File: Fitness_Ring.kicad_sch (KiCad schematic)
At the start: 14 parts, among them U1 NRF52832-QFAA-R, U2 MAX30102, U3 MIC5370-SGYMT-TR, U4 MCP73831-2-OT, U5 TXS0102DQE

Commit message: made changes to schematic
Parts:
- added C10: 1.2pF, symbol Device:C
- added C11: 0.1uF, symbol Device:C
- added C12, C9: 100pF, symbol Device:C
- added C6: 100nF, symbol Device:C
- added C7, C8: 12pF, symbol Device:C
- added E1: 2450AT18B100E, 2450AT18B100E:XDCR_2450AT18B100E, symbol New_Library:2450AT18B100E
- added L1: 3.3nH, symbol Device:L
- added L2: 2.7nH, symbol Device:L
- added R4, R5, R6, R7: 4.7K, symbol Device:R
- added U6: MAX30205MTA_, MAX30205MTA_:SON65P300X300X80-9N, symbol New_Library:MAX30205MTA_
- added Y1: 32.768kHz, symbol Device:Crystal
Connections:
- net VSS is gone; now on net GND: U1.31 (VSS), U1.45 (VSS)
- net +3.3V: now also C11.2, R4.1, R5.1, R6.2, U6.8 (VDD)
- net GND: now also U4.2 (V_{SS}), C10.2, C11.1, C6.2, C7.2, C8.2, C9.2, L2.1, R7.2, U6.4 (GND), U6.5 (A2), U6.6 (A1), U6.7 (A0), U6.9 (EP)
- net SCL: now also U1.15 (P0_12), R5.2, U6.2 (SCL); no longer MT1.13 (AP_SCL/AP_SCLK), R1.2
- net SDA: now also U1.14 (P0_11), R4.2, U6.1 (SDA); no longer MT1.14 (AP_SDA/AP_SDIO/AP_SDI), R2.2
- net at U4.5 (PROG): now also R7.1
- net SCLK: now reaches U1.28 (P0_23)
- net SCLK: now also MT1.13 (AP_SCL/AP_SCLK), R1.2
- net SDI: now reaches U1.29 (P0_24)
- net SDI: now also MT1.14 (AP_SDA/AP_SDIO/AP_SDI), R2.2
- net at U1.30 (ANT): now also C10.1, L1.1, L2.2
- net at U1.33 (DEC3): now also C9.1
- net at U1.34 (XC1): now also C7.1, Y1.1
- net at U1.35 (XC2): now also C8.1, Y1.2
- net at U1.46 (DEC4): now also C6.1
- net INT1 renamed INT_PPG
- net INT_PPG: no longer MT1.4 (INT1/INT)
- new net: R6.1, U6.3 (OS)
- new net: E1.1, L1.2
- new net INT_IMU_TAP: MT1.4 (INT1/INT)
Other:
- note added: "PPG"
- note added: "Temp Sensor"
- note removed: "Sensors"
- moved on the sheet: C1, C5, R3, U1, U2, U4, U5

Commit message: Finalized the schematic
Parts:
- removed C12: 100pF, symbol Device:C
- added C13: 4.7uF, symbol Device:C
- added D1: LED, symbol Device:LED
- added R8: 470, symbol Device:R
- E1: footprint 2450AT18B100E:XDCR_2450AT18B100E -> Fitness:Battery
- MT1: footprint ICM-42670-P:XDCR_ICM-42670-P -> Fitness:ICM-42670-P
- U1: footprint NRF52832-QFAA-R:QFN40P600X600X90-49N -> Fitness:nRF52832
- U3: footprint TMLF-6_MT_MCH -> Fitness:MIC5370
- U6: footprint MAX30205MTA_:SON65P300X300X80-9N -> Fitness:MAX30205
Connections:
- net +3.3V: no longer C2.1, U3.1 (VIN)
- net GND: now also C13.1
- net INT_IMU_TAP: now also U1.4 (P0_02/AIN0)
- net SCL: now also MT1.13 (AP_SCL/AP_SCLK), R1.2
- net SDA: now also MT1.14 (AP_SDA/AP_SDIO/AP_SDI), R2.2
- net at U4.1 (STAT): now also R8.1
- net VBAT: now reaches U4.3 (V_{BAT})
- net VBAT: now also C2.1, U3.1 (VIN)
- net +5V: now reaches U4.4 (V_{DD})
- net +5V: now also C13.2, D1.2 (A)
- removed net SCLK: MT1.13 (AP_SCL/AP_SCLK), R1.2, U1.28 (P0_23)
- removed net SDI: MT1.14 (AP_SDA/AP_SDIO/AP_SDI), R2.2, U1.29 (P0_24)
- new net: D1.1 (K), R8.2
- no-connect marks 5 -> 39
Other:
- note added: "Charger"
- note added: "nRF52832"
- moved on the sheet: C11, R6, R7, U4, U6

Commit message: Finished adding all the footprints and updated the PCB from schematic
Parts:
- removed R1, R2: R, symbol Device:R
- C1, C10, C11, C13, C2, C3, C4, C5, C6, C7, C8, C9: footprint (none) -> Capacitor_SMD:C_0402_1005Metric
- D1: footprint (none) -> LED_SMD:LED_0603_1608Metric
- L1, L2: footprint (none) -> Inductor_SMD:L_0402_1005Metric
- R3, R4, R5, R6, R7, R8: footprint (none) -> Resistor_SMD:R_0402_1005Metric
- Y1: footprint (none) -> Crystal:Crystal_SMD_2012-2Pin_2.0x1.2mm

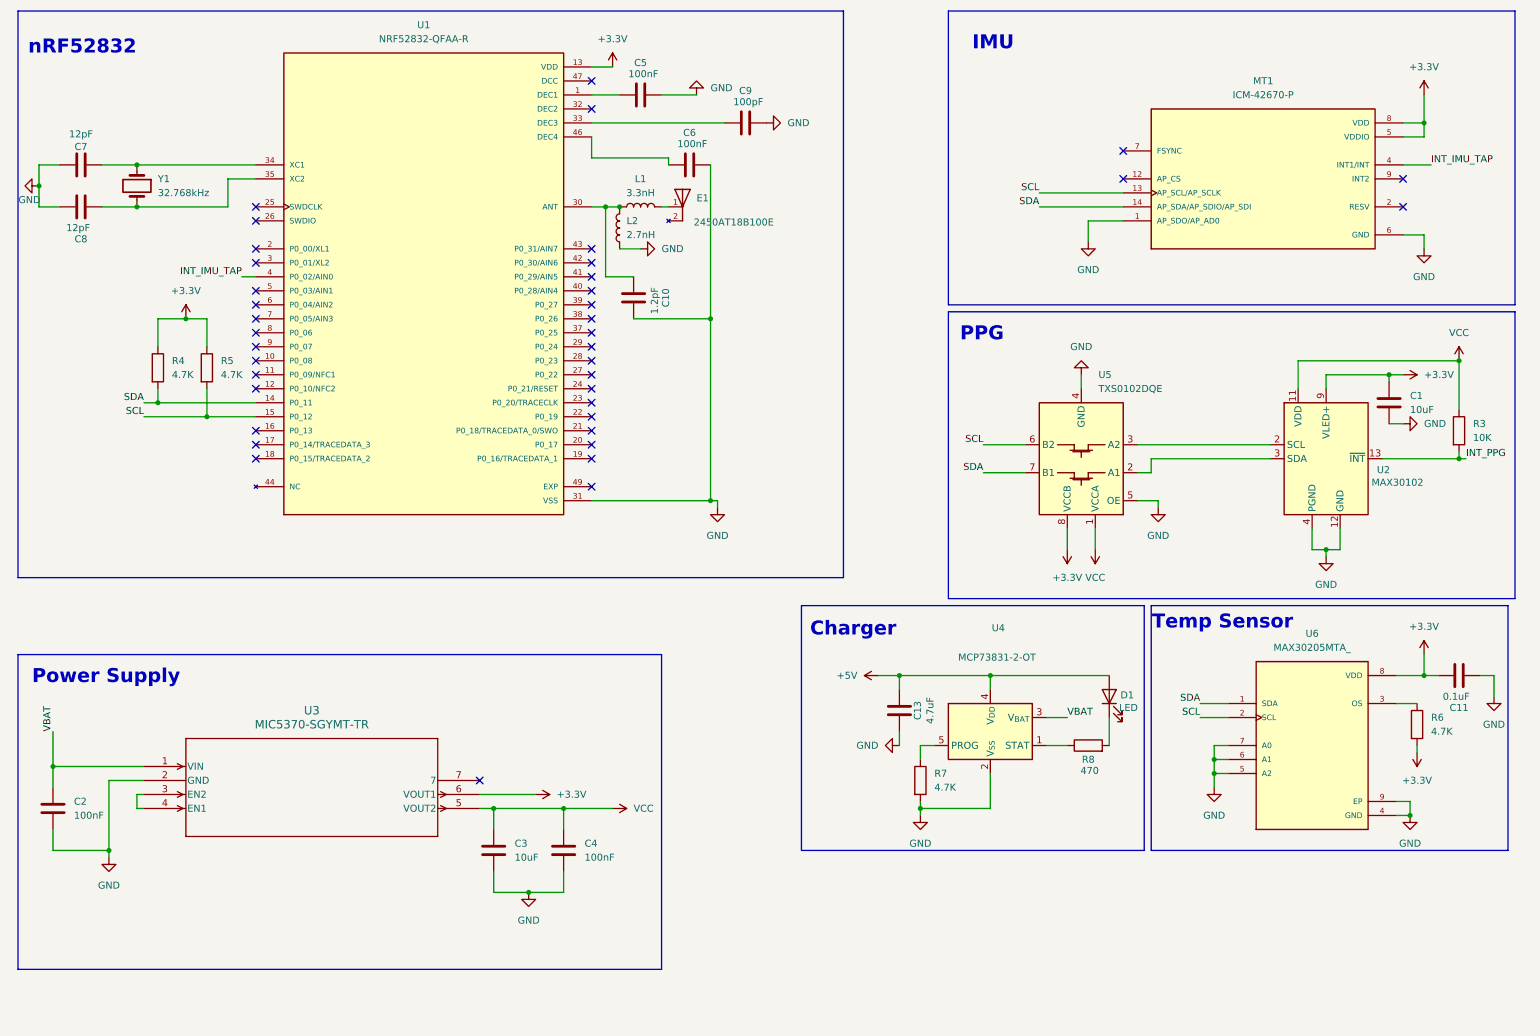
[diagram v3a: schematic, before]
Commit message: placed all components on the PCB, need to make sure to change schematic so that MAX30102 has its own separate I2C bus
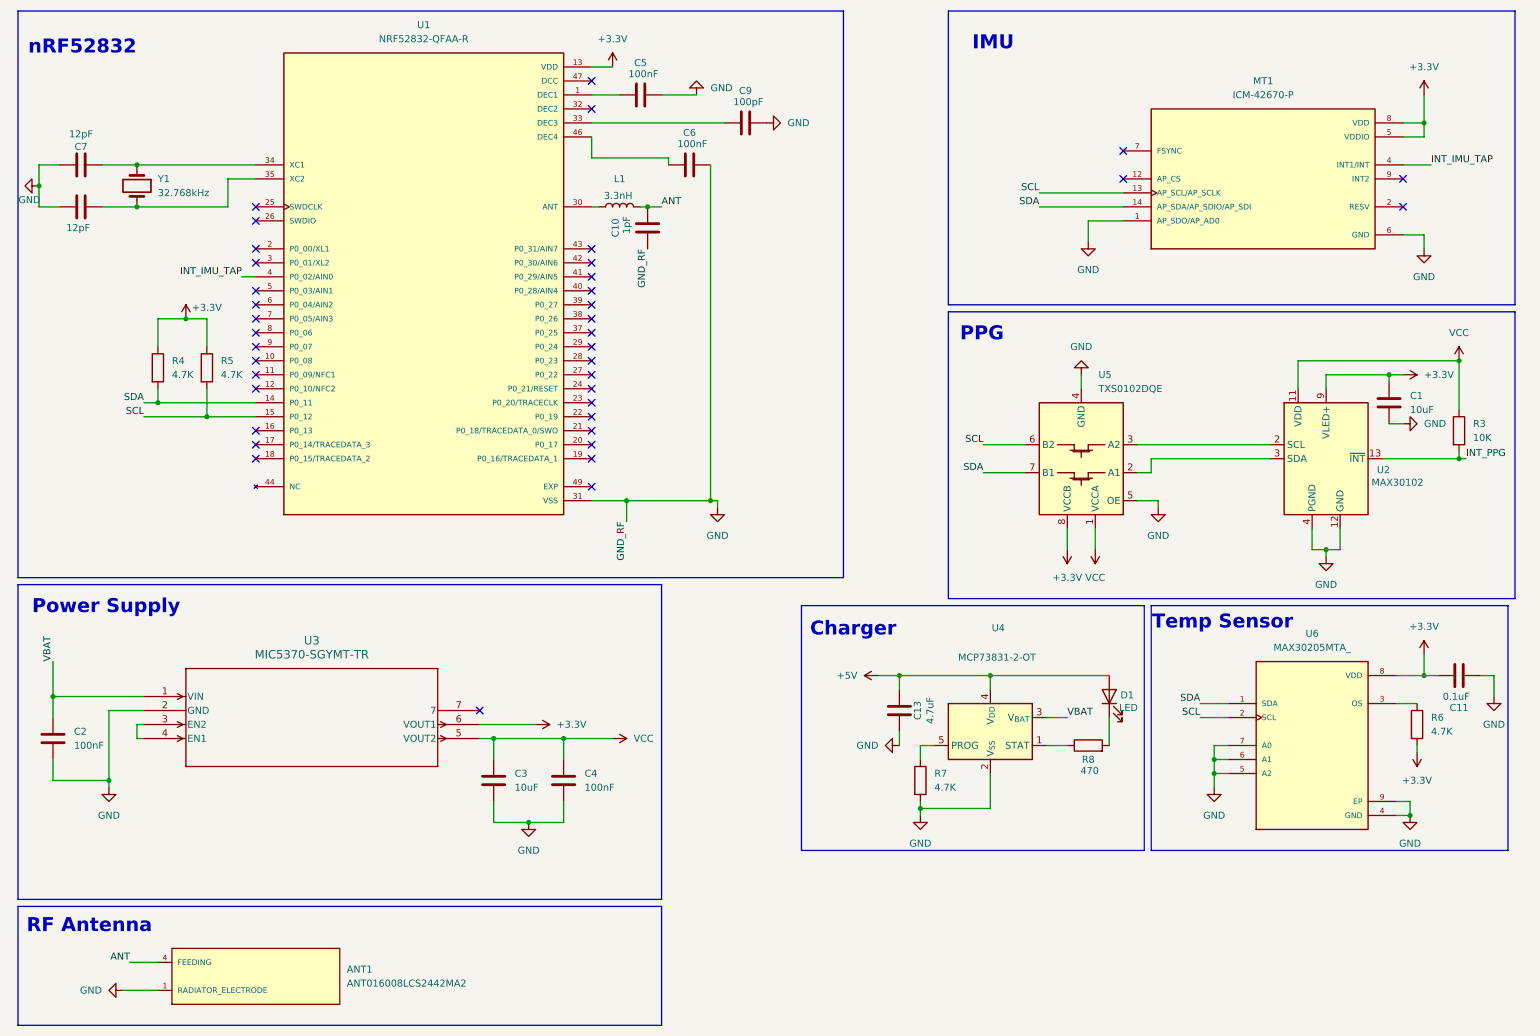
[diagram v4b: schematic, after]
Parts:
- removed E1: 2450AT18B100E, Fitness:Battery, symbol New_Library:2450AT18B100E
- removed L2: 2.7nH, Inductor_SMD:L_0402_1005Metric, symbol Device:L
- added ANT1: ANT016008LCS2442MA2, Fitness:ANT_ANT016008LCS2442MA2, symbol New_Library:ANT016008LCS2442MA2
- C10: value 1.2pF -> 1pF
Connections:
- net GND: now also C10.1, ANT1.1 (RADIATOR_ELECTRODE); no longer C10.2
- net at L1.1, U1.30 (ANT): no longer C10.1
- net ANT: now reaches L1.2
- net ANT: now also C10.2, ANT1.4 (FEEDING)
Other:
- note added: "RF Antenna"
- moved on the sheet: C2, C3, C4, U3

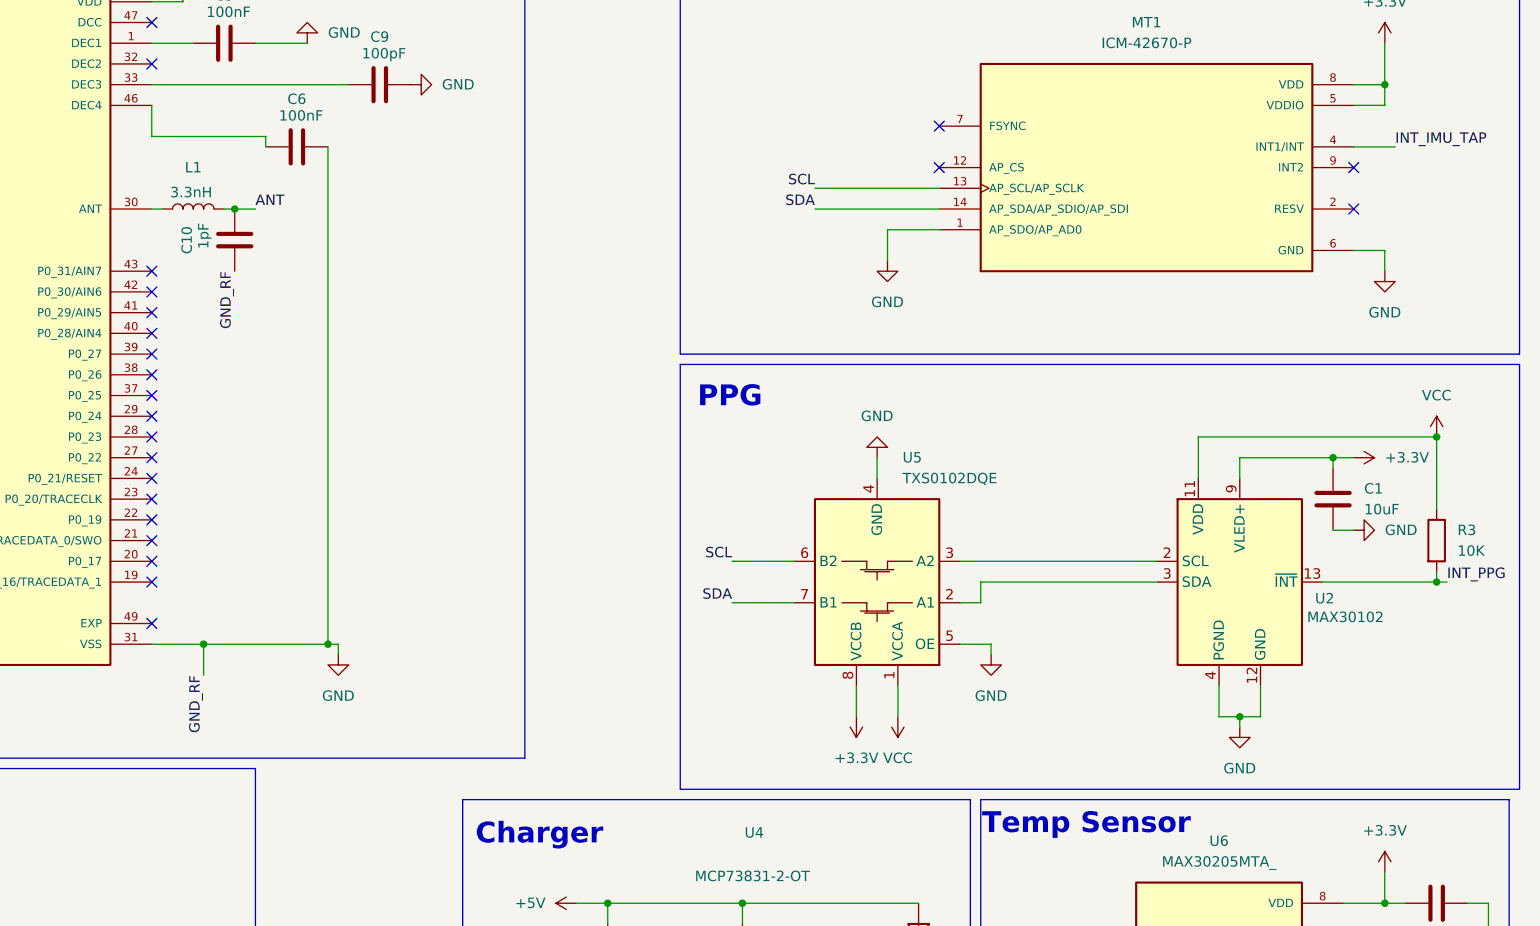
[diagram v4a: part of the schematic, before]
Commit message: Removed the level translator as we do not need it anymore, switching to a flex PCB with two layers to fix the trace impedance width problem while not going up too much in cost, will work on that next time
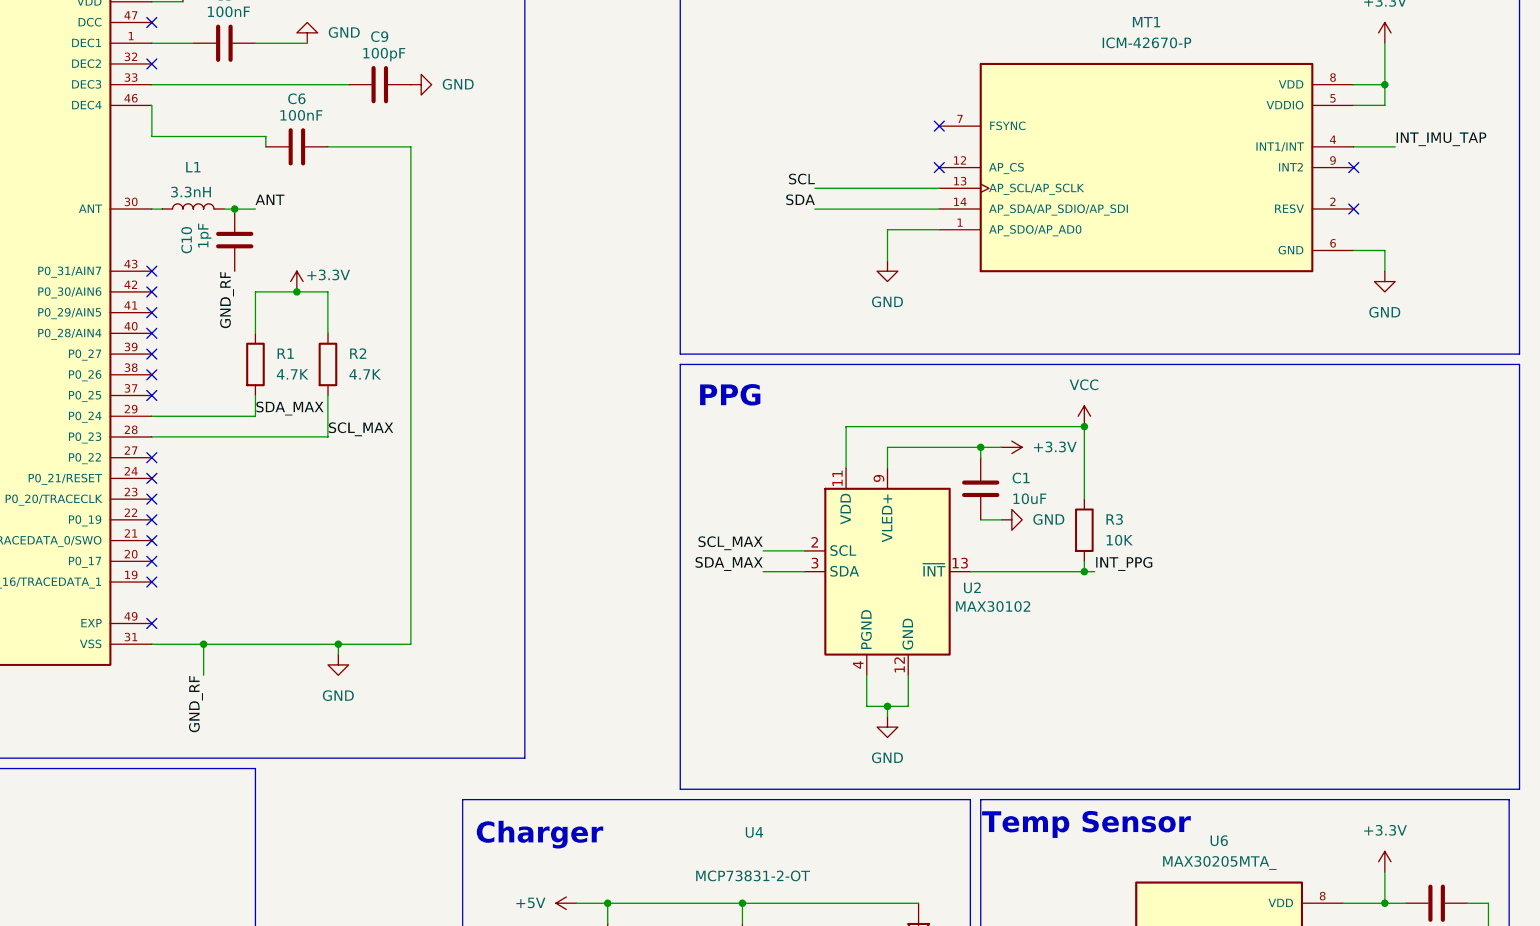
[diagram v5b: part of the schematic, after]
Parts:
- removed U5: TXS0102DQE, Package_SON:X2SON-8_1.4x1mm_P0.35mm, symbol Logic_LevelTranslator:TXS0102DQE
- added R1, R2: 4.7K, Resistor_SMD:R_0402_1005Metric, symbol Device:R
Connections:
- net +3.3V: now also R1.1, R2.1
- net SDA_MAX: now reaches U2.3 (SDA)
- net SDA_MAX: now also U1.29 (P0_24), R1.2
- net SCL_MAX: now reaches U2.2 (SCL)
- net SCL_MAX: now also U1.28 (P0_23), R2.2
- no-connect marks 39 -> 37
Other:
- moved on the sheet: C1, R3, U2
